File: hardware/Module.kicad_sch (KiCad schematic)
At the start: 119 parts, among them J1 Jack, J10 Jack, J11 Jack, J12 Jack, J13 Micro_SD, J14 NW_B, J15 Jack, J16 Jack, J17 Power, J18 Jack, J19 Jack, J2 OLED, J20 SW_B, J21 NW_A, J22 SW_A, J23 NE_A, J3 NE_B, J4 Jack, J5 Jack, J6 Jack, J7 Jack, J8 Jack, J9 Jack, SW1 Encoder, U1 TL074, U2 TL074, U3 TL074, U4 MCP6004, U5 MCP6002, U7 LM4040C10

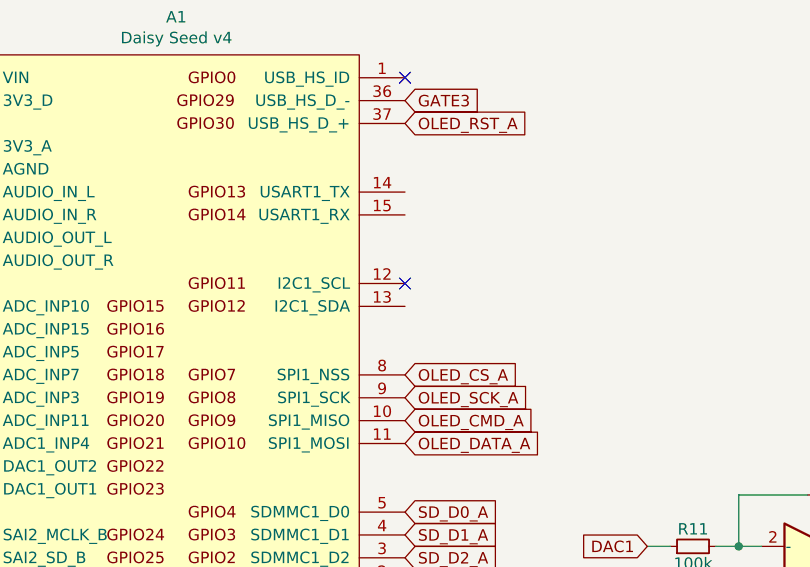
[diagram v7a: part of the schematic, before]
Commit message: Add extension socket
It could be hotwired to unused pins of daisy using wires.

Signed-off-by: Petr Horacek <hrck@protonmail.com>
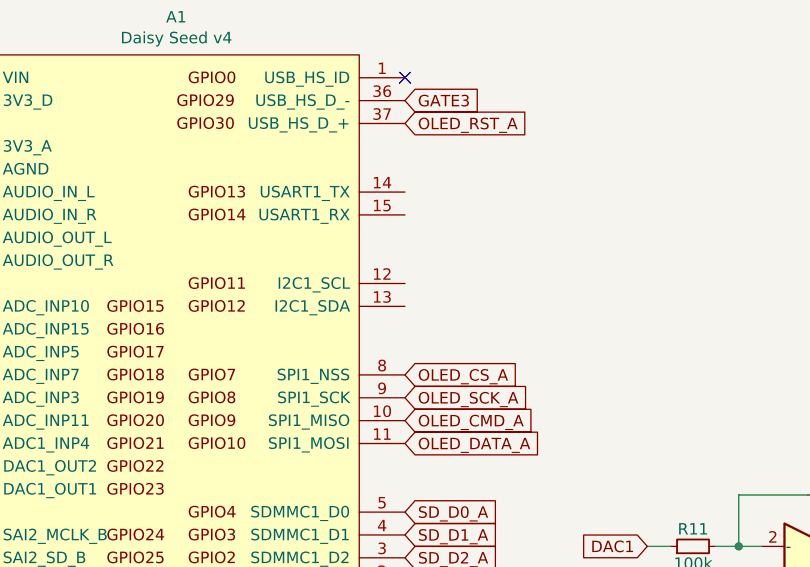
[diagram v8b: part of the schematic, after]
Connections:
- no-connect marks 15 -> 14
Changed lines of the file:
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@@
   (no_connect (at 191.77 150.114))
   (no_connect (at 191.516 196.215))
-  (no_connect (at 107.315 60.452))
   (no_connect (at 191.77 172.72))
   (no_connect (at 373.38 200.787))
@@
   (symbol (lib_id "power:+3.3VA") (at 47.117 145.923 270) (unit 1)
     (in_bom yes) (on_board yes)
-    (property "Reference" "#PWR?" (id 0) (at 43.307 145.923 0)
+    (property "Reference" "#PWR0104" (id 0) (at 43.307 145.923 0)
       (effects (font (size 1.27 1.27)) hide)
     )
@@
   (symbol (lib_id "power:+3.3VA") (at 106.553 146.304 270) (unit 1)
     (in_bom yes) (on_board yes)
-    (property "Reference" "#PWR?" (id 0) (at 102.743 146.304 0)
+    (property "Reference" "#PWR0103" (id 0) (at 102.743 146.304 0)
       (effects (font (size 1.27 1.27)) hide)
     )
@@
       (reference "#PWR0102") (unit 1) (value "+3.3V") (footprint "")
     )
-    (path "/6e7a06f4-e193-4588-880c-5ca44d724b97"
-      (reference "#PWR?") (unit 1) (value "+3.3VA") (footprint "")
-    )
     (path "/b44d5b5c-eafb-4692-b7ef-c83c742340eb"
-      (reference "#PWR?") (unit 1) (value "+3.3VA") (footprint "")
+      (reference "#PWR0103") (unit 1) (value "+3.3VA") (footprint "")
+    )
+    (path "/6e7a06f4-e193-4588-880c-5ca44d724b97"
+      (reference "#PWR0104") (unit 1) (value "+3.3VA") (footprint "")
     )
     (path "/00000000-0000-0000-0000-000062372793"
